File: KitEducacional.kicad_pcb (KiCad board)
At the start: 2 copper layers, 131 x 102 mm, 45 parts, among them J1 Serial 1, J10 D4, J11 D5, J12 D6, J13 D7, J14 D8, J15 D9, J16 D10, J17 D11, J18 D12, J19 D13, J2 Serial 2, J20 D14, J21 D15, J22 A0, J23 A1, J24 A2, J25 A3, J26 A4, J27 A5, J28 A6, J29 A7, J3 Serial 3, J4 I²C, J5 SPI, J6 D0, J7 D1, J8 D2, J9 D3, SW1 SW_Push, SW2 SW_Push, SW3 SW_Push, SW4 SW_Push, SW5 SW_Push, U1 ESP32-WROOM-32

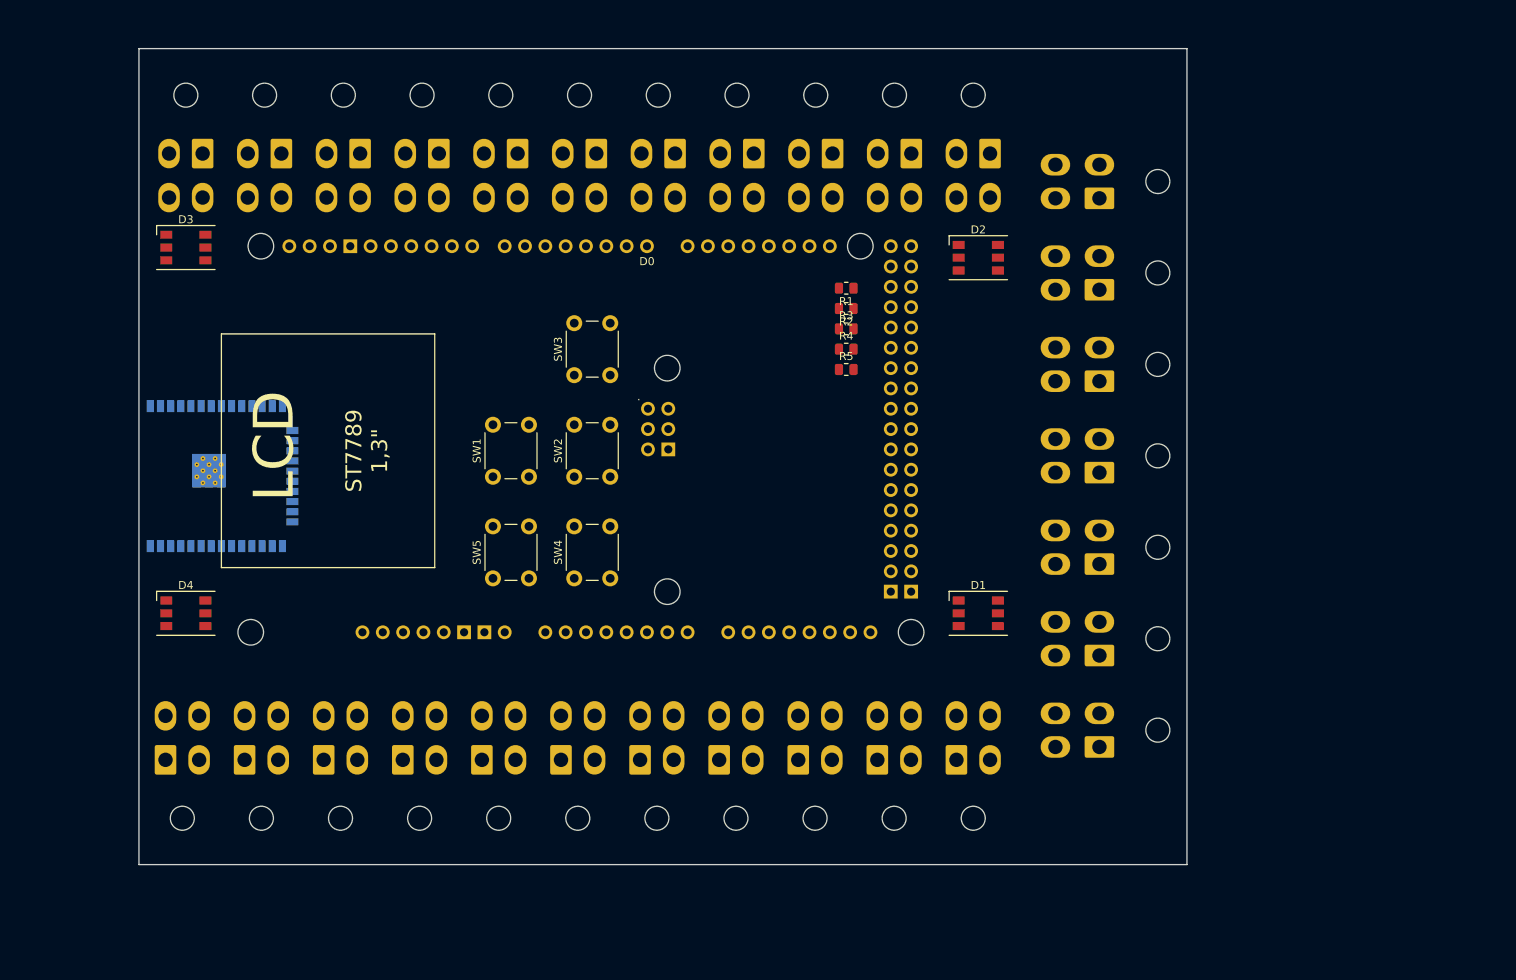
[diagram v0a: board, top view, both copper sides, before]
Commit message: go back to molex Nano Fit
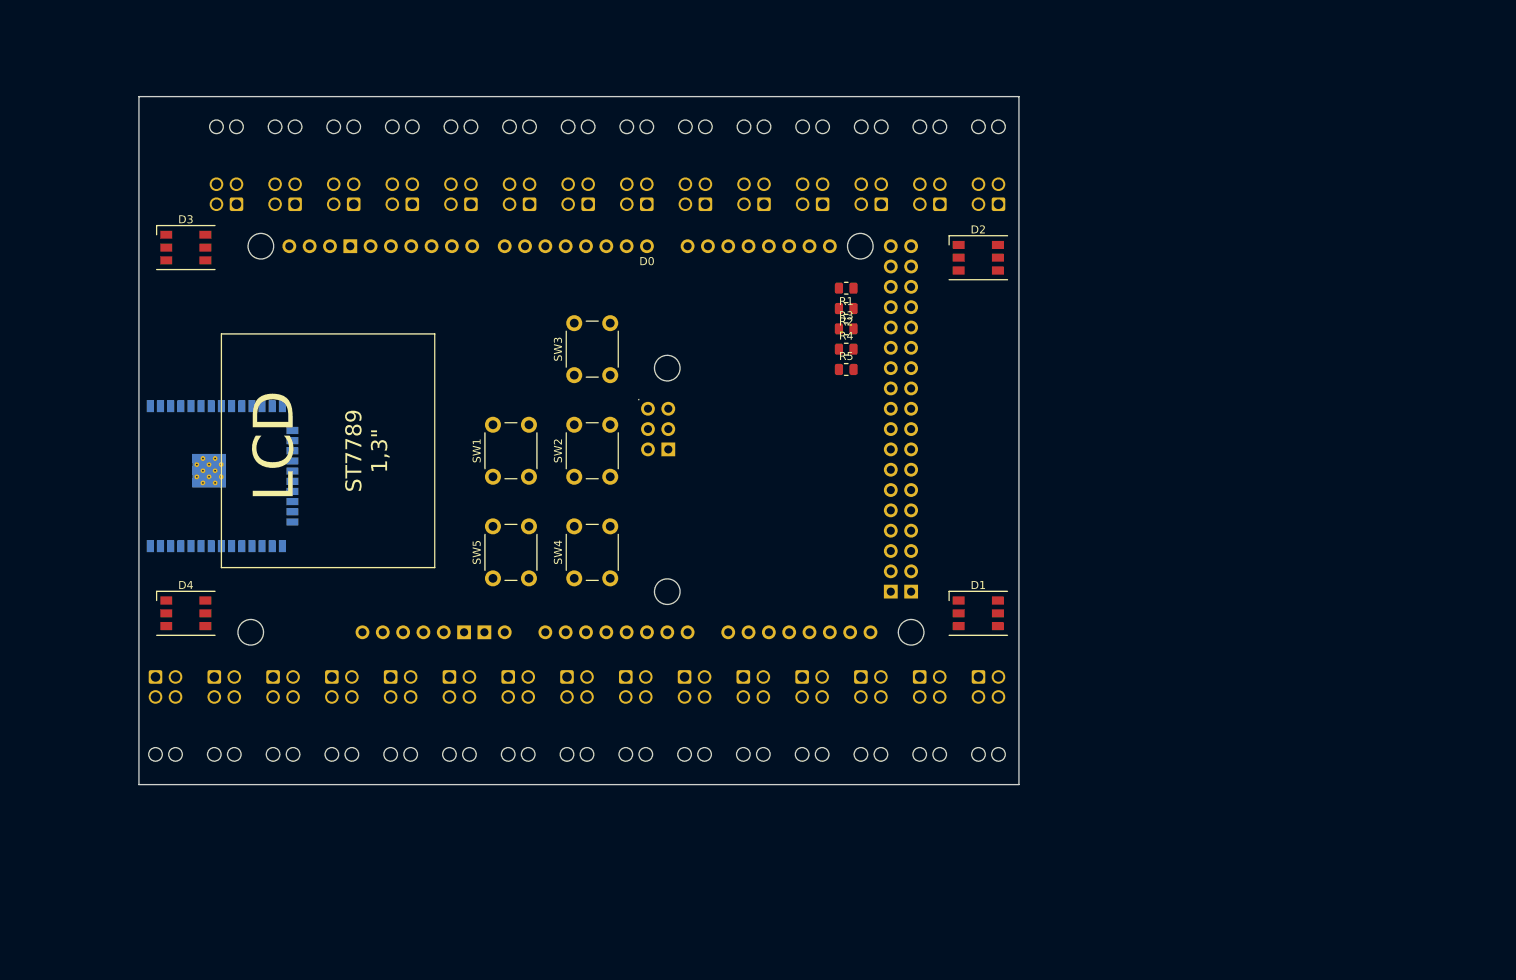
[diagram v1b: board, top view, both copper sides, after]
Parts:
- J1, J10, J11, J12, J13, J14, J15, J16, J17, J18, J19, J2, J20, J21, J22, J23, J24, J25, J26, J27, J28, J29, J3, J4, J5, J6, J7, J8, J9: footprint Connector_Molex:Molex_Mini-Fit_Jr_5569-04A2_2x02_P4.20mm_Horizontal -> Connector_Molex:Molex_Nano-Fit_105314-xx04_2x02_P2.50mm_Horizontal
- moved J29 118.0 mm to (104.2, 119.7), turned to -90 degrees
- moved J14 111.5 mm to (111.5, 119.7), turned to -90 degrees
- moved J1 102.1 mm to (207.0, 119.7), turned to -90 degrees
- moved J27 101.1 mm to (121.6, 60.6)
- moved J12 99.3 mm to (126.2, 119.7), turned to -90 degrees
- moved J26 93.2 mm to (128.9, 60.6)
- moved J10 81.7 mm to (140.9, 119.7), turned to -90 degrees
- moved J25 72.5 mm to (136.3, 60.6), turned to 90 degrees
- moved J16 62.9 mm to (202.2, 60.6), turned to 90 degrees
- moved J9 57.0 mm to (148.2, 119.7), turned to -90 degrees
- moved J23 48.1 mm to (150.9, 60.6), turned to 90 degrees
- moved J5 43.8 mm to (177.6, 119.7), turned to -90 degrees
- moved J22 38.9 mm to (158.2, 60.6), turned to 90 degrees
- moved J18 38.7 mm to (187.5, 60.6), turned to 90 degrees
- moved J17 36.2 mm to (194.9, 60.6), turned to 90 degrees
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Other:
- board size 131 x 102 mm -> 110 x 86 mm

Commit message: goto mini-fit
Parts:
- added BZ1: Buzzer, Buzzer_Beeper:Buzzer_12x9.5RM7.6, F.Cu at (186.7, 108.6)
- J1, J10, J11, J12, J13, J14, J15, J16, J17, J18, J19, J2, J20, J21, J22, J23, J24, J25, J26, J27, J28, J29, J3, J4, J5, J6, J7, J8, J9: footprint Connector_Molex:Molex_Nano-Fit_105314-xx04_2x02_P2.50mm_Horizontal -> Connector_Molex:Molex_Mini-Fit_Jr_5569-04A2_2x02_P4.20mm_Horizontal
- moved J13 152.3 mm to (263.4, 72.0), turned to 90 degrees
- moved J27 148.0 mm to (240.9, 148.2), turned to 180 degrees
- moved J26 137.7 mm to (240.9, 140.9), turned to 180 degrees
- moved J25 127.5 mm to (240.9, 133.5), turned to 180 degrees
- moved J24 117.3 mm to (240.9, 126.2), turned to 180 degrees
- moved J14 114.4 mm to (211.5, 64.1), turned to 90 degrees
- moved J4 102.5 mm to (108.3, 51.6), turned to 180 degrees
- moved J23 99.5 mm to (239.3, 106.2)
- moved J8 77.1 mm to (119.6, 51.5), turned to 180 degrees
- moved J7 75.6 mm to (130.4, 51.5), turned to 180 degrees
- moved J21 74.0 mm to (184.8, 132.1), turned to 0 degrees
- moved J22 73.0 mm to (173.4, 132.1), turned to 0 degrees
- moved J10 72.2 mm to (162.8, 50.9), turned to 180 degrees
- moved J12 71.1 mm to (196.2, 132.1), turned to 0 degrees
- moved J20 69.3 mm to (211.4, 118.3)
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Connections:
- A1 pad D23: unconnected-(A1-PadD23) -> D23
- A1 pad D25: unconnected-(A1-PadD25) -> D25
- A1 pad D27: unconnected-(A1-PadD27) -> D27
- A1 pad D29: unconnected-(A1-PadD29) -> D29
- A1 pad D31: unconnected-(A1-PadD31) -> D31
- A1 pad D33: unconnected-(A1-PadD33) -> D33
- A1 pad D34: unconnected-(A1-PadD34) -> D34
- A1 pad D35: unconnected-(A1-PadD35) -> D35
- A1 pad D36: unconnected-(A1-PadD36) -> D36
- A1 pad D37: unconnected-(A1-PadD37) -> D37
- A1 pad D38: unconnected-(A1-PadD38) -> D38
- A1 pad D39: unconnected-(A1-PadD39) -> D39
- A1 pad D40: unconnected-(A1-PadD40) -> D40
- A1 pad D41: unconnected-(A1-PadD41) -> D41
- A1 pad D44: unconnected-(A1-PadD44) -> D44
- A1 pad D45: unconnected-(A1-PadD45) -> D45
- A1 pad D46: unconnected-(A1-PadD46) -> D46
- A1 pad D47: unconnected-(A1-PadD47) -> D47
- J13 pad 1: unconnected-(J13-Pin_1-Pad1) -> D23
- J13 pad 2: unconnected-(J13-Pin_2-Pad2) -> D25
- J14 pad 1: unconnected-(J14-Pin_1-Pad1) -> D27
- J14 pad 2: unconnected-(J14-Pin_2-Pad2) -> D29
- J15 pad 1: unconnected-(J15-Pin_1-Pad1) -> D31
- J15 pad 2: unconnected-(J15-Pin_2-Pad2) -> D33
- J16 pad 1: unconnected-(J16-Pin_1-Pad1) -> D35
- J16 pad 2: unconnected-(J16-Pin_2-Pad2) -> D37
- J17 pad 1: unconnected-(J17-Pin_1-Pad1) -> D39
- J17 pad 2: unconnected-(J17-Pin_2-Pad2) -> D41
- J18 pad 1: unconnected-(J18-Pin_1-Pad1) -> D34
- J18 pad 2: unconnected-(J18-Pin_2-Pad2) -> D36
- J19 pad 1: unconnected-(J19-Pin_1-Pad1) -> D38
- J19 pad 2: unconnected-(J19-Pin_2-Pad2) -> D40
- J20 pad 1: unconnected-(J20-Pin_1-Pad1) -> D45
- J20 pad 2: unconnected-(J20-Pin_2-Pad2) -> D47
- J21 pad 1: unconnected-(J21-Pin_1-Pad1) -> D44
- J21 pad 2: unconnected-(J21-Pin_2-Pad2) -> D46
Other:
- board size 110 x 86 mm -> 120 x 106 mm
